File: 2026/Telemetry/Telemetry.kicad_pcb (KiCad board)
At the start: 4 copper layers, 62.5 x 22.6 mm, 46 parts, among them IC1 ESP32-S3-WROOM-1-N8R8, IC2 CP2102N-A02-GQFN28, IC3 TLP175A_TPL,E, IC4 TPS2116DRLR, IC5 MIC37100-3.3WS, J1 USB4730-GF-A, J2 Conn_01x04_Socket, Q1 MMBT2222LT1G, Q2 MMBT2222LT1G, U1 USBLC6-2SC6, U2 SN65HVD230

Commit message: Telemetry finalization
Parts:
- removed C4: 1uF, Capacitor_SMD:C_0603_1608Metric
- removed LED1: GREEN, LED_SMD:LED_0603_1608Metric
- removed R2: 220, Resistor_SMD:R_0603_1608Metric
- removed TP1: ST_5V, TestPoint:TestPoint_Pad_1.5x1.5mm
- added G***: LOGO, LOGO, B.Cu at (97.3, 62.2)
- added G***: LOGO, LOGO, B.Cu at (87.2, 87.6)
- added G***: LOGO, LOGO, B.Cu at (78.0, 88.4)
- added G***: LOGO, LOGO, B.Cu at (109.0, 89.6)
- added H1: M2, MountingHole:MountingHole_2.2mm_M2, F.Cu at (127.5, 99.5)
- added H2: M2, MountingHole:MountingHole_2.2mm_M2, F.Cu at (77.4, 83.0)
- added LED3: 150060GS75000, SDM_MiscFootprint:LEDC1608X80N, F.Cu at (122.3, 101.5)
- IC1: footprint SDM_MiscFootprint:ESP32S3WROOM1N8R8 -> SDM_MiscFootprint:ESP32S3WROOM1UN8R8
- J1: footprint SDM_MiscFootprint:USB4730GFA -> SDM_MiscFootprint:USB_C_Receptacle_16P
- R15: value 10k -> 5.05
- moved C10 13.2 mm to (82.7, 92.1)
- moved R16 11.4 mm to (79.9, 99.9), turned to 180 degrees
- moved IC3 10.5 mm to (79.4, 96.5), turned to 180 degrees
- moved C11 10.2 mm to (82.7, 89.1), turned to 90 degrees
- moved J2 9.76 mm to (72.5, 87.5), turned to -90 degrees
- moved D1 7.66 mm to (74.0, 99.8), turned to -90 degrees
- moved LED2 7.28 mm to (122.3, 99.6), turned to 180 degrees
- moved R12 6.98 mm to (76.9, 99.9), turned to 180 degrees
- moved R7 6.83 mm to (122.0, 84.7), turned to -90 degrees
- moved R17 6.41 mm to (119.3, 99.6), turned to 0 degrees
- moved R8 4.97 mm to (117.3, 83.9), turned to 0 degrees
- moved R15 4.46 mm to (119.3, 101.1), turned to 180 degrees
- moved U2 4.39 mm to (78.2, 91.2), turned to 180 degrees
- moved IC1 4.24 mm to (94.0, 91.0)
- moved C5 4.21 mm to (117.3, 85.4)
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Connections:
- IC1 pad 10: /CAN_TERM -> unconnected-(IC1-IO17-Pad10)
- IC1 pad 11: /CAN_CTX -> unconnected-(IC1-IO18-Pad11)
- IC1 pad 13: unconnected-(IC1-IO19-Pad13) -> /CAN_TERM
- IC1 pad 25: unconnected-(IC1-IO48-Pad25) -> /USER_LED
- IC1 pad 28: /USER_LED -> unconnected-(IC1-IO35-Pad28)
- IC1 pad 4: unconnected-(IC1-IO4-Pad4) -> /CAN_CTX
- IC4 pad 8: /ST -> unconnected-(IC4-ST-Pad8)
- J2 pad 2: /CAN1- -> /CAN-
- J2 pad 3: /CAN1+ -> /CAN+
- R15 pad 1: +5V -> Net-(LED3-A)
- R15 pad 2: /ST -> /USER_LED
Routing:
- net GND: track 19.5 -> 65.2 mm, vias 31 -> 28
- net /CAN_TERM: track 15.9 -> 2.67 mm
- net /CAN_RTX: track 16.7 -> 7.07 mm, vias 2 -> 0
- net VCC: track 51.3 -> 59.8 mm, vias 0 -> 1
- net /CAN_CTX: track 13.7 -> 6.39 mm, vias 2 -> 0
- net /USER_LED: track 13.1 -> 19.9 mm
- net Net-(U2-Rs): track 1.72 -> 8.33 mm, vias 0 -> 2
- net Net-(IC2-VBUS): track 4.85 -> 10.1 mm
- net /ST: track 4.55 -> 0.00 mm
- net /PROG_D+: track 5.98 -> 2.90 mm, vias 0 -> 2
- net /PROG_D-: track 4.23 -> 7.19 mm, vias 2 -> 0
- net Net-(Q1-B): track 2.44 -> 5.32 mm, vias 0 -> 2
- net +5V: track 12.8 -> 10.1 mm
- net /GPIO0: track 10.5 -> 8.25 mm
- net Net-(IC2-DTR): track 11.9 -> 14.1 mm
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- added copper zone on F.Cu, net GND
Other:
- board size 62.5 x 22.6 mm -> 61.5 x 22.5 mm
- board text added: "JLCJLCJLCJLC"
- board text added: "SDM-26 DAQ Telemetry V1.0"
- board text added: "Telemetry was promised to engine 3000 years ago"
- board text added: "boy..Well this was planned in October They advertise 2km over wifi From the"
- board text added: "leader It's giving broke"
- board text added: "the xiao to the HaLow Engine gets brutally packet mogged by the SDM DAQ"
- board text added: "transfer to the Teensy to"

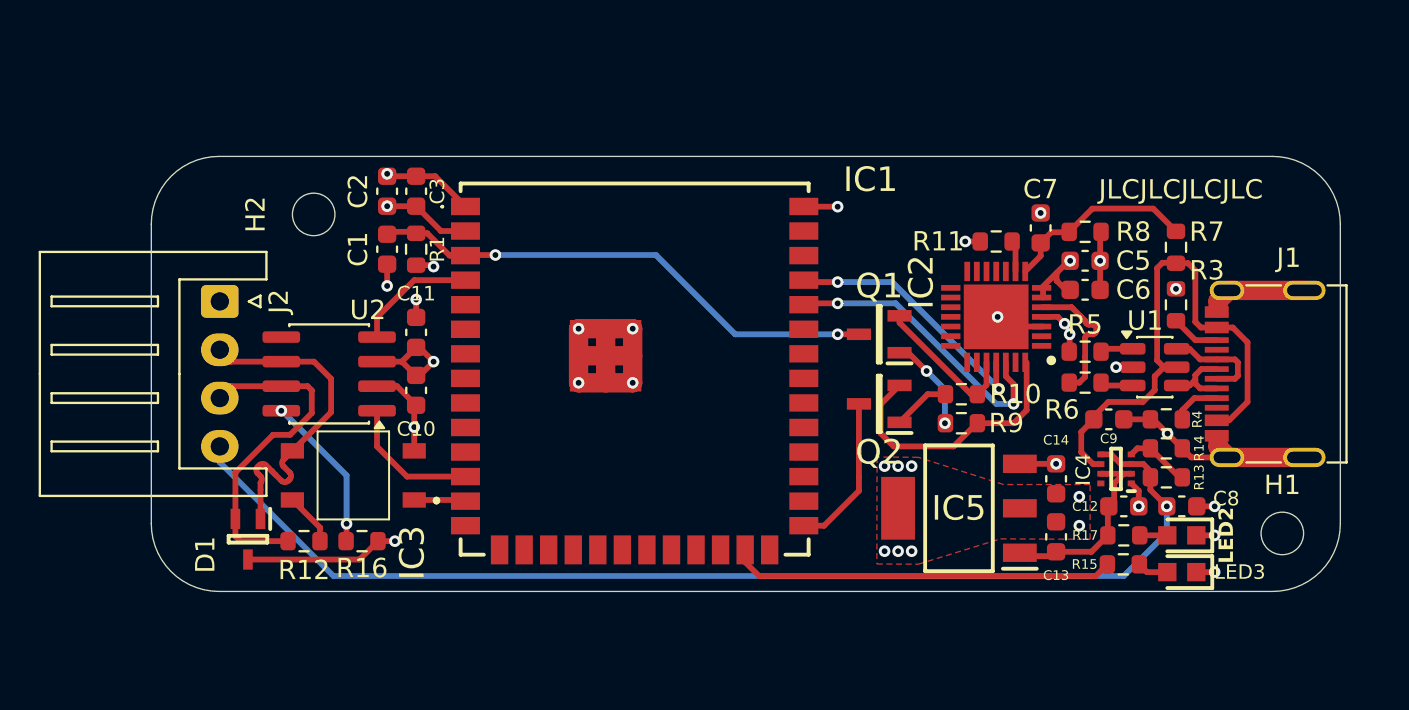
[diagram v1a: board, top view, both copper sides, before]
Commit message: Added RF amplifier to telemetry board
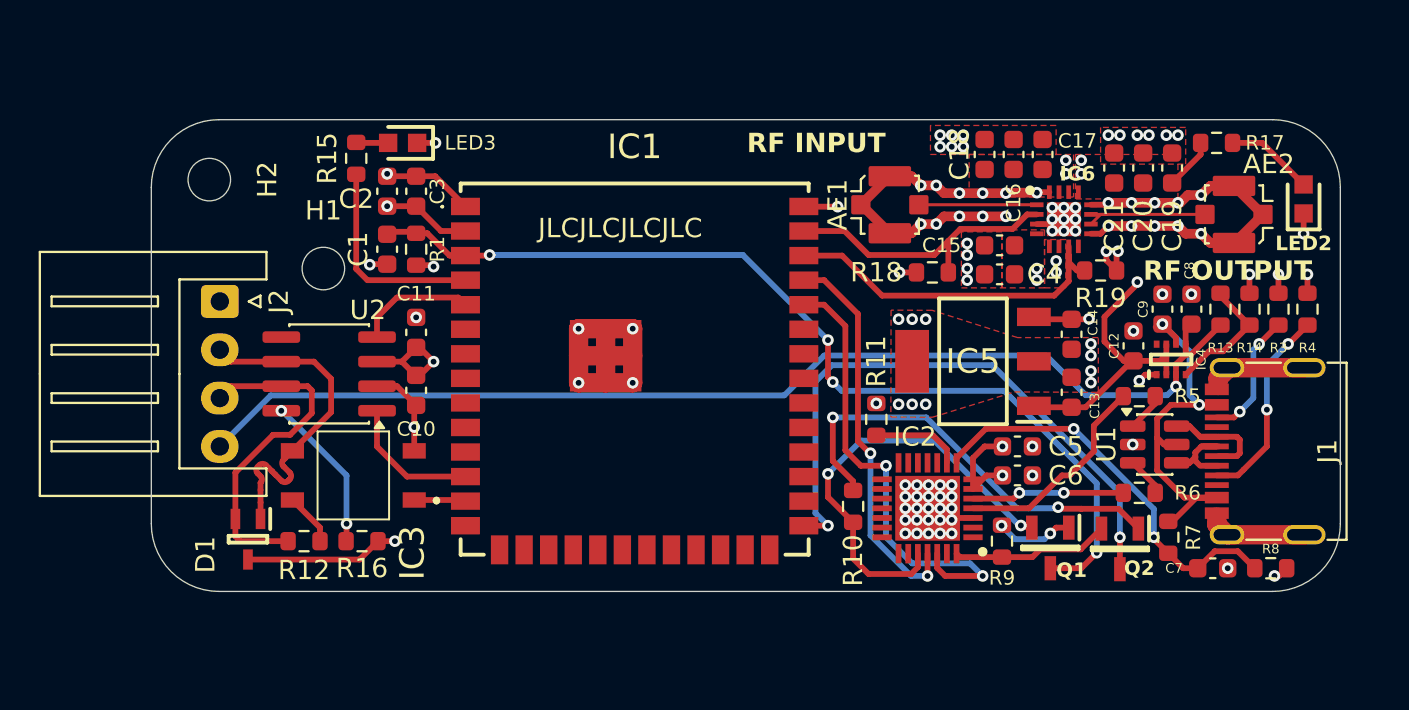
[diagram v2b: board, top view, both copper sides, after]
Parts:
- added AE1: UFL, Connector_Coaxial:U.FL_Molex_MCRF_73412-0110_Vertical, F.Cu at (107.2, 82.5)
- added AE2: UFL, Connector_Coaxial:U.FL_Molex_MCRF_73412-0110_Vertical, F.Cu at (125.0, 83.0)
- added C15: 22pF, Capacitor_SMD:C_0603_1608Metric, F.Cu at (112.9, 84.6)
- added C16: 100nF, Capacitor_SMD:C_0603_1608Metric, F.Cu at (113.6, 79.9)
- added C17: 22pF, Capacitor_SMD:C_0603_1608Metric, F.Cu at (115.1, 79.9)
- added C18: 4.7uF, Capacitor_SMD:C_0603_1608Metric, F.Cu at (112.1, 79.9)
- added C19: 10uF, Capacitor_SMD:C_0603_1608Metric, F.Cu at (121.8, 80.6)
- added C20: 100nF, Capacitor_SMD:C_0603_1608Metric, F.Cu at (120.3, 80.6)
- added C21: 22pF, Capacitor_SMD:C_0603_1608Metric, F.Cu at (118.8, 80.6)
- added C4: 100nF, Capacitor_SMD:C_0603_1608Metric, F.Cu at (112.9, 86.1)
- added IC6: SE2576L-R, SDM_MiscFootprint:QFN50P300X300X90-17L-D, F.Cu at (116.2, 83.2)
- added R18: 0, Resistor_SMD:R_0603_1608Metric, F.Cu at (109.4, 86.0)
- added R19: 10k, Resistor_SMD:R_0603_1608Metric, F.Cu at (118.1, 85.9)
- R17: value 68 -> 100
- moved H1 51.5 mm to (77.9, 85.8)
- moved LED3 46.0 mm to (82.0, 79.3)
- moved R15 44.9 mm to (79.6, 80.1), turned to -90 degrees
- moved R17 20.9 mm to (124.1, 79.3)
- moved R8 19.9 mm to (126.9, 101.3)
- moved C7 19.7 mm to (123.9, 101.3), turned to 0 degrees
- moved LED2 18.5 mm to (128.6, 82.2), turned to 90 degrees
- moved R7 15.0 mm to (121.6, 99.7), turned to 90 degrees
- moved Q2 14.5 mm to (119.1, 100.3), turned to -90 degrees
- moved Q1 14.2 mm to (115.5, 100.2), turned to -90 degrees
- moved R11 11.1 mm to (106.5, 93.6), turned to 90 degrees
- moved IC2 10.5 mm to (109.2, 98.2)
- moved C5 10.2 mm to (113.8, 95.0)
- moved C6 10.2 mm to (113.8, 96.5)
- moved C8 10.2 mm to (122.8, 87.9), turned to -90 degrees
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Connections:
- IC1 pad 25: /USER_LED -> unconnected-(IC1-IO48-Pad25)
- IC1 pad 38: unconnected-(IC1-IO2-Pad38) -> /AMP_DET
- IC1 pad 39: unconnected-(IC1-IO1-Pad39) -> /AMP_EN
- IC1 pad 4: /CAN_CTX -> /USER_LED
- IC1 pad 5: unconnected-(IC1-IO5-Pad5) -> /CAN_CTX
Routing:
- net GND: track 65.2 -> 99.7 mm, vias 28 -> 109
- net /GPIO0: track 8.25 -> 31.8 mm, vias 0 -> 2
- net /CHIP_PU: track 26.6 -> 49.5 mm, vias 2 -> 4
- net Net-(Q2-B): track 2.98 -> 22.4 mm, vias 0 -> 2
- net /AMP_DET: track 0.00 -> 18.0 mm
- net /AMP_EN: track 0.00 -> 15.1 mm
- net Net-(IC2-RTS): track 7.76 -> 22.6 mm, vias 0 -> 2
- net Net-(IC2-VBUS): track 10.1 -> 20.9 mm, vias 0 -> 2
- net /USER_LED: track 19.9 -> 10.8 mm
- net /U0RXD: track 15.3 -> 24.2 mm
- net /PROG_D+: track 2.90 -> 11.0 mm, vias 2 -> 0
- net +5V: track 10.1 -> 18.0 mm, vias 0 -> 7
- net Net-(J1-CC1): track 2.52 -> 10.4 mm, vias 0 -> 2
- net VBUS: track 27.5 -> 20.4 mm, vias 0 -> 2
- net Net-(AE2-A): track 0.00 -> 6.81 mm
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- added copper zone on F.Cu, net +5V
- added copper zone on In2.Cu, net +5V
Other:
- board size 61.5 x 22.5 mm -> 61.5 x 24.4 mm
- board text added: "RF INPUT"
- board text added: "RF OUTPUT"
- board text added: "boy..Well this was planned in October They advertise 2km over wifi From"
- board text added: "the transfer to the Teensy"
- board text added: "to the xiao to the HaLow Engine gets brutally packet mogged by the DAQ"
- board text removed: "boy..Well this was planned in October They advertise 2km over wifi From the"
- board text removed: "the xiao to the HaLow Engine gets brutally packet mogged by the SDM DAQ"
- board text removed: "transfer to the Teensy to"
